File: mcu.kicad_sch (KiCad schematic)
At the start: 41 parts, among them U1 STM32U5G9ZJTxQ, Y1 NX2016SA-16MHZ-EXS00A-CS07826, Y2 NX2012SA-32.768K-STD-MUB-1

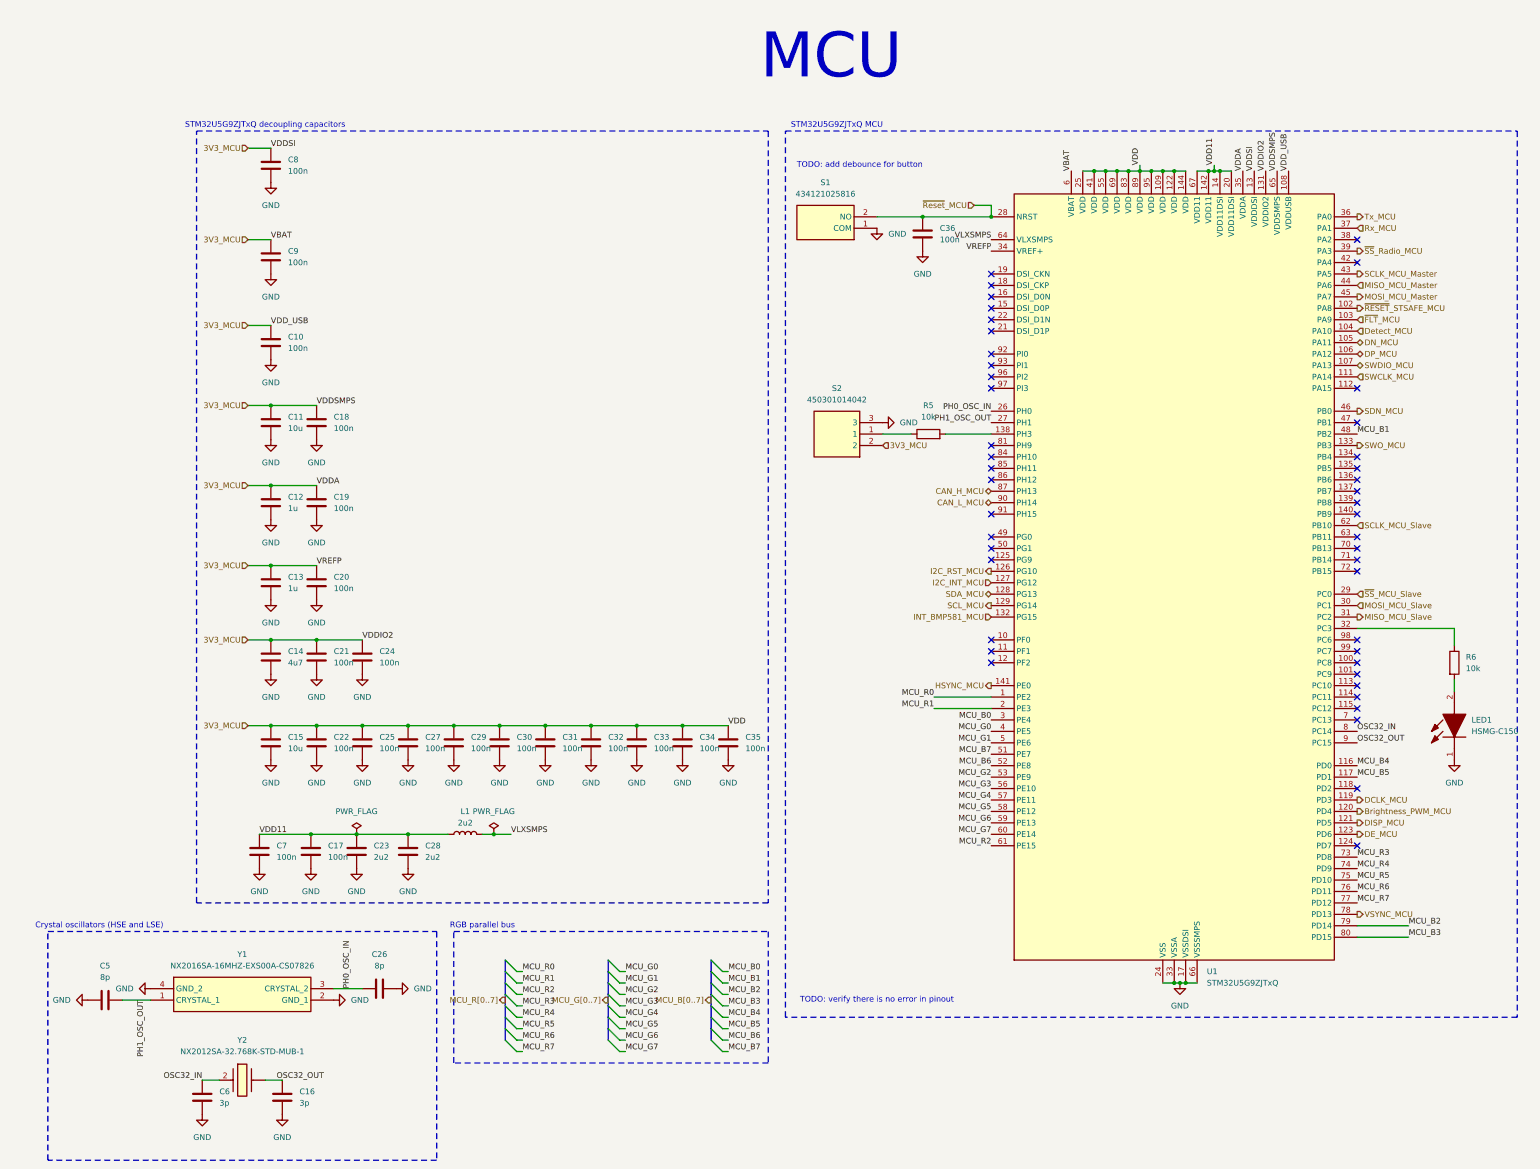
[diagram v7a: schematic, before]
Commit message: Homogenation of symbols
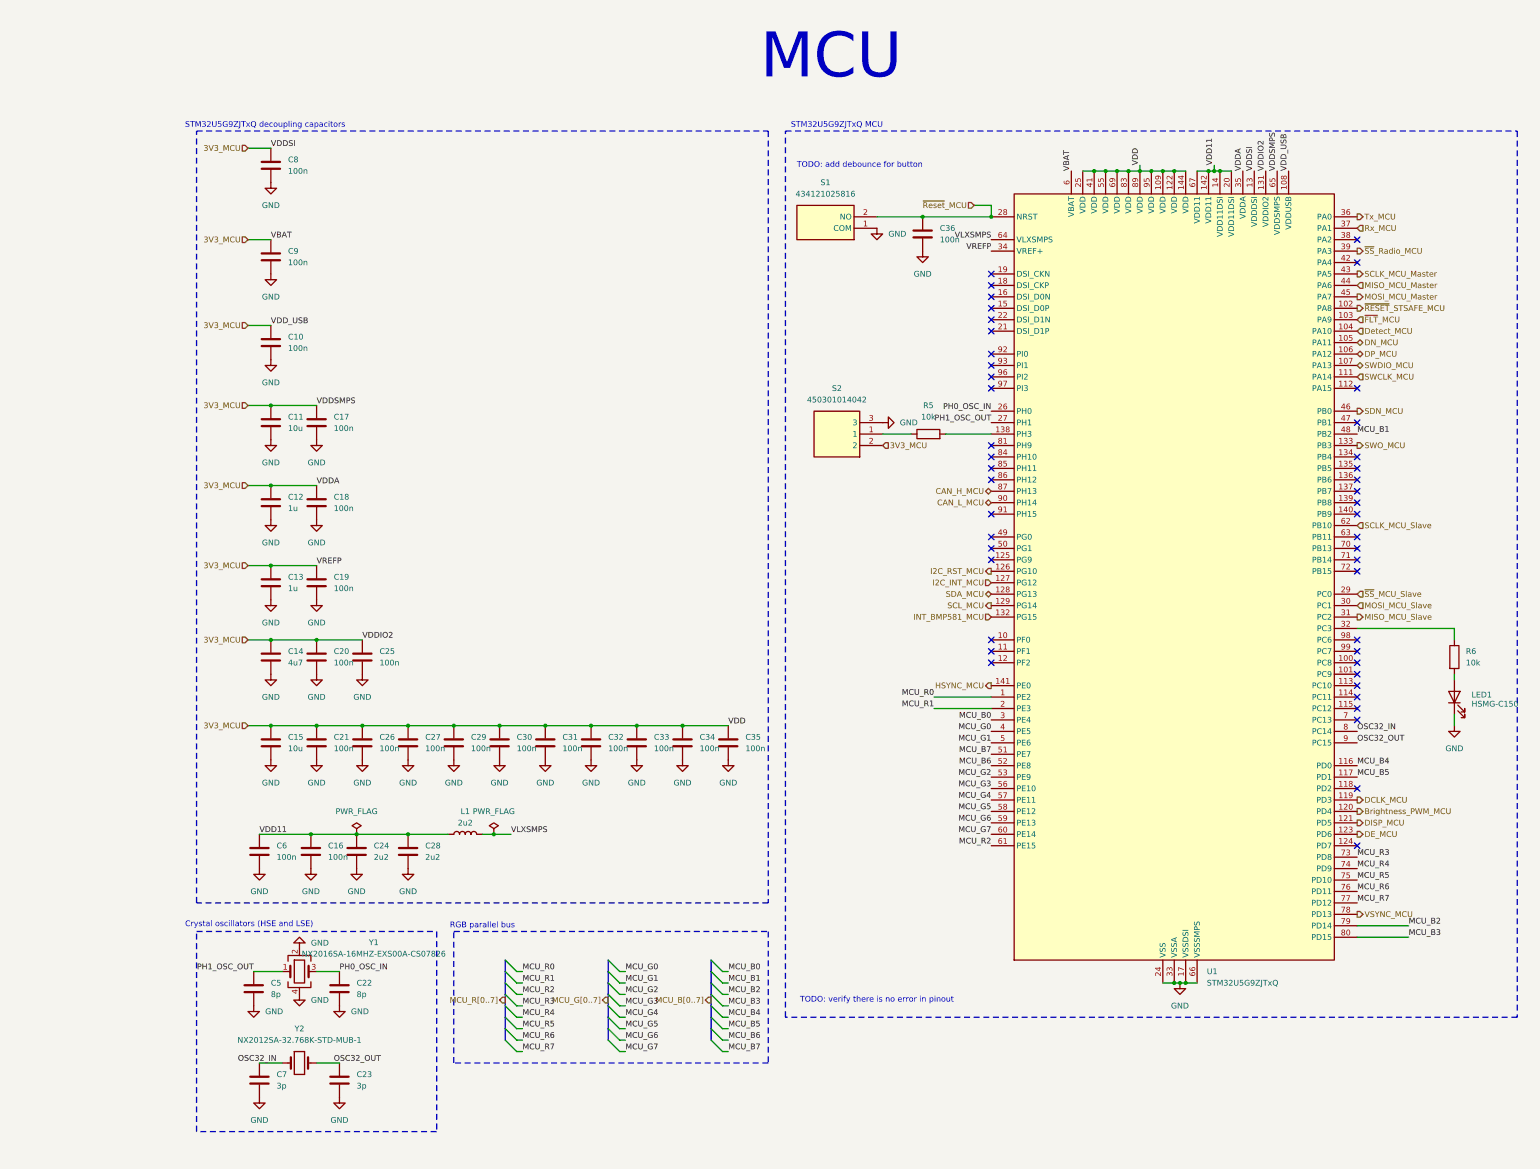
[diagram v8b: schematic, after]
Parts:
- LED1: symbol weather-station-poc-sym:HSMG-C150 -> Device:LED
- Y1: symbol weather-station-poc-sym:NX2016SA-16MHZ-EXS00A-CS07826 -> Device:Crystal_GND24
- Y2: symbol weather-station-poc-sym:NX2012SA-32.768K-STD-MUB-1 -> Device:Crystal
- renumbered C17 to C16, C18 to C17, C19 to C18, C20 to C19, C21 to C20, C22 to C21, C26 to C22, C16 to C23, C23 to C24, C24 to C25, C25 to C26, C7 to C6, C6 to C7
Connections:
- net GND: now also C22.1; no longer C22.2
- net OSC32_IN: now also Y2.1; no longer Y2.2 (CRYSTAL_2)
- net OSC32_OUT: now also Y2.2; no longer Y2.
- net PH0_OSC_IN: now also C22.2; no longer C22.1
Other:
- moved on the sheet: C22, C23, C5, C7, R6
